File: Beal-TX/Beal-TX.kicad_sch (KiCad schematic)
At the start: 0 parts

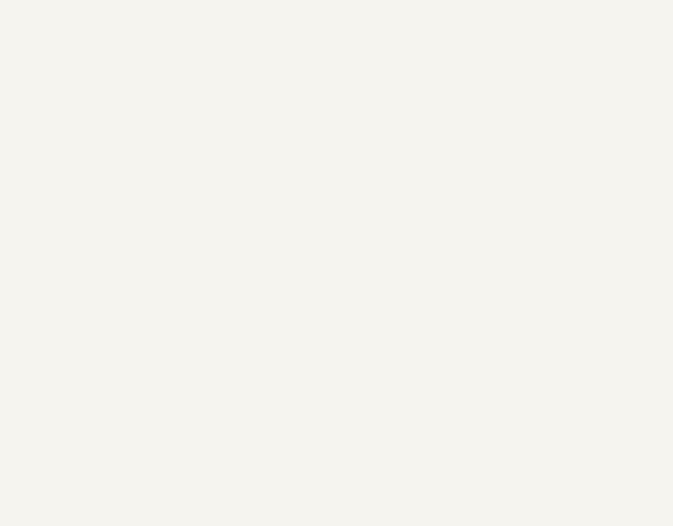
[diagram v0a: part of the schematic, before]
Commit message: Beal TX: Address some issues found during prototyping phase
Basically, the prototyping phase has highlighted some issues.
The major one is about the power delivered by an USB-C battery
is not enough to safely driver the valve.
The power after 9V decrease to about 5V, and the 5V from battery
fall to 2.0V.

One way for fixing it is using super capacitor.
This adds an extra cost to the BOM, and, I am not about its
duration regarding the operating conditions.

Because of the cost and the doubt about the longevity,
I would like to evaluate other solutions.
But, we also need to move forward so I made some changes to
power to make it more configurable so we could later try external
battery with a BMS, with different voltage with or without the booster.
By default we will have the super capacitor but we could slit main and
super capacitor board and plug a battery or any power source instead.

A minor change also introduced by this commit is adding testpoints.
Since the hardware an the software is not yet done, testpoints will
be very useful for debugging.

Signed-off-by: Alexandre Bailon <abailon@baylibre.com>
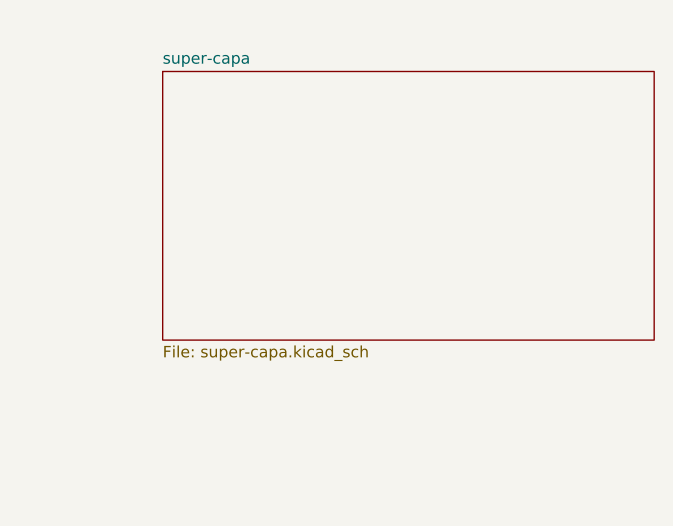
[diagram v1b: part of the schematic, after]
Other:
- added sheet super-capa (super-capa.kicad_sch)
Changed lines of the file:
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@@
+	)
+	(sheet
+		(at 163.195 33.655)
+		(size 54.61 29.845)
+		(exclude_from_sim no)
+		(in_bom yes)
+		(on_board yes)
+		(dnp no)
+		(fields_autoplaced yes)
+		(stroke
+			(width 0.1524)
+			(type solid)
+		)
+		(fill
+			(color 0 0 0 0)
+		)
+		(property "Sheetname" "super-capa"
+			(at 163.195 32.9434 0)
+			(show_name no)
+			(do_not_autoplace no)
+			(effects
+				(font
+					(size 1.27 1.27)
+				)
+				(justify left bottom)
+			)
+		)
+		(property "Sheetfile" "super-capa.kicad_sch"
+			(at 163.195 64.0846 0)
+			(show_name no)
+			(do_not_autoplace no)
+			(effects
+				(font
+					(size 1.27 1.27)
+				)
+				(justify left top)
+			)
+		)
+		(instances
+			(project "Beal-TX"
+				(path "/5ecf7ddf-d623-4591-9f28-acf618ce627e"
+					(page "5")
+				)
+			)
+		)
 	)
 	(sheet

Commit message: Beal-TX: Remove changes previoulsy done regarding done regarding battery tests
I made some measurement on comptitor product and finaly,
the signal to control the valve is not that bad.
I have decided to just add a capacitor and to remove all the
tests features added by previous commit.

This also tries to address some potential issues and does some
improvements such as increasing traces for VBUS and +9V.

Signed-off-by: Alexandre Bailon <abailon@baylibre.com>
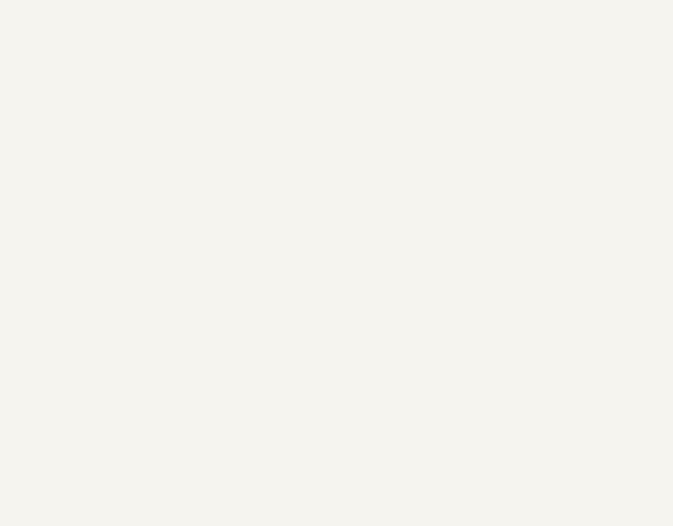
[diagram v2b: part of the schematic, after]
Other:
- removed sheet super-capa
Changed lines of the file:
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@@
-	)
-	(sheet
-		(at 163.195 33.655)
-		(size 54.61 29.845)
-		(exclude_from_sim no)
-		(in_bom yes)
-		(on_board yes)
-		(dnp no)
-		(fields_autoplaced yes)
-		(stroke
-			(width 0.1524)
-			(type solid)
-		)
-		(fill
-			(color 0 0 0 0)
-		)
-		(property "Sheetname" "super-capa"
-			(at 163.195 32.9434 0)
-			(show_name no)
-			(do_not_autoplace no)
-			(effects
-				(font
-					(size 1.27 1.27)
-				)
-				(justify left bottom)
-			)
-		)
-		(property "Sheetfile" "super-capa.kicad_sch"
-			(at 163.195 64.0846 0)
-			(show_name no)
-			(do_not_autoplace no)
-			(effects
-				(font
-					(size 1.27 1.27)
-				)
-				(justify left top)
-			)
-		)
-		(instances
-			(project "Beal-TX"
-				(path "/5ecf7ddf-d623-4591-9f28-acf618ce627e"
-					(page "5")
-				)
-			)
-		)
 	)
 	(sheet
